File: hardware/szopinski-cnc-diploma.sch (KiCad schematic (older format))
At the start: 26 parts, among them J1 Barrel_Jack, J2 Conn_02x08_Odd_Even, J3 AVR-ISP-10, J4 Conn_01x04, J5 Conn_01x04, J6 Conn_01x04, J7 Conn_01x04, U1 ATmega328P-PU, U2 L7805, U3 DRV8825, U4 DRV8825, U5 DRV8825, U6 DRV8825, Y1 20 MHz

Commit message: Add custom symbol and footprint to project
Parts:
- removed U3, U4, U5, U6: DRV8825, Package_DIP:DIP-16_W15.24mm, symbol Driver_Motor:DRV8825
- added U3, U4, U5, U6: DRV8825, szopinski-cnc-diploma:DIP-16_W15.24mm, symbol drv8825:DRV8825
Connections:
- net +18V: now also U3.16 (VCC), U4.16 (VCC), U5.16 (VCC), U6.16 (VCC)
- net +5V: now also U3.2 (M0), U3.3 (M1), U3.4 (M2), U3.5 (~RST), U3.6 (~SLP), U4.2 (M0), U4.3 (M1), U4.4 (M2), U4.5 (~RST), U4.6 (~SLP), U5.2 (M0), U5.3 (M1), U5.4 (M2), U5.5 (~RST), U5.6 (~SLP), U6.2 (M0), U6.3 (M1), U6.4 (M2), U6.5 (~RST), U6.6 (~SLP)
- net DIR_X: now also U3.8 (DIR)
- net DIR_Y: now also U5.8 (DIR), U6.8 (DIR)
- net DIR_Z: now also U4.8 (DIR)
- net ENABLE_XY: now also U3.1 (~EN), U5.1 (~EN), U6.1 (~EN)
- net ENABLE_Z: now also U4.1 (~EN)
- net GND: now also U3.15 (GNDmot), U3.9 (GND), U4.15 (GNDmot), U4.9 (GND), U5.15 (GNDmot), U5.9 (GND), U6.15 (GNDmot), U6.9 (GND)
- net STEP_X: now also U3.7 (STEP)
- net STEP_Y: now also U5.7 (STEP), U6.7 (STEP)
- net STEP_Z: now also U4.7 (STEP)
- net at J4.1 (Pin_1): now also U3.14 (B2)
- net at J4.2 (Pin_2): now also U3.13 (B1)
- net at J4.3 (Pin_3): now also U3.12 (A1)
- net at J4.4 (Pin_4): now also U3.11 (A2)
- net at J6.1 (Pin_1): now also U5.14 (B2)
- net at J6.2 (Pin_2): now also U5.13 (B1)
- net at J6.3 (Pin_3): now also U5.12 (A1)
- net at J6.4 (Pin_4): now also U5.11 (A2)
- net at J5.1 (Pin_1): now also U4.14 (B2)
- net at J5.2 (Pin_2): now also U4.13 (B1)
- net at J5.3 (Pin_3): now also U4.12 (A1)
- net at J5.4 (Pin_4): now also U4.11 (A2)
- net at J7.1 (Pin_1): now also U6.14 (B2)
- net at J7.2 (Pin_2): now also U6.13 (B1)
- net at J7.3 (Pin_3): now also U6.12 (A1)
- net at J7.4 (Pin_4): now also U6.11 (A2)
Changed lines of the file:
@@
 NoConn ~ 9000 5050
 NoConn ~ 9000 2450
-$Comp
-L Driver_Motor:DRV8825 U3
-U 1 1 63106504
-P 6850 1700
-F 0 "U3" H 7528 1096 50  0000 L CNN
-F 1 "DRV8825" H 7528 1005 50  0000 L CNN
-F 2 "Package_DIP:DIP-16_W15.24mm" H 7550 1100 50  0001 C CNN
-F 3 "" H 7550 1100 50  0001 C CNN
-	1    6850 1700
-	1    0    0    -1
-$EndComp
-$Comp
-L Driver_Motor:DRV8825 U5
-U 1 1 6310708B
-P 9750 1700
-F 0 "U5" H 10428 1096 50  0000 L CNN
-F 1 "DRV8825" H 10428 1005 50  0000 L CNN
-F 2 "Package_DIP:DIP-16_W15.24mm" H 10450 1100 50  0001 C CNN
-F 3 "" H 10450 1100 50  0001 C CNN
-	1    9750 1700
-	1    0    0    -1
-$EndComp
-$Comp
-L Driver_Motor:DRV8825 U6
-U 1 1 63107951
-P 9750 4300
-F 0 "U6" H 10428 3696 50  0000 L CNN
-F 1 "DRV8825" H 10428 3605 50  0000 L CNN
-F 2 "Package_DIP:DIP-16_W15.24mm" H 10450 3700 50  0001 C CNN
-F 3 "" H 10450 3700 50  0001 C CNN
-	1    9750 4300
-	1    0    0    -1
-$EndComp
-$Comp
-L Driver_Motor:DRV8825 U4
-U 1 1 63108532
-P 6850 4300
-F 0 "U4" H 7528 3696 50  0000 L CNN
-F 1 "DRV8825" H 7528 3605 50  0000 L CNN
-F 2 "Package_DIP:DIP-16_W15.24mm" H 7550 3700 50  0001 C CNN
-F 3 "" H 7550 3700 50  0001 C CNN
-	1    6850 4300
-	1    0    0    -1
-$EndComp
 Text Label 5250 5400 2    50   Italic 0
 ENABLE_Z
@@
 NoConn ~ 2900 3300
 NoConn ~ 4900 4000
+$Comp
+L drv8825:DRV8825 U3
+U 1 1 631C04A9
+P 6850 1700
+F 0 "U3" H 7528 1096 50  0000 L CNN
+F 1 "DRV8825" H 7528 1005 50  0000 L CNN
+F 2 "szopinski-cnc-diploma:DIP-16_W15.24mm" H 7550 1100 50  0001 C CNN
+F 3 "" H 7550 1100 50  0001 C CNN
+	1    6850 1700
+	1    0    0    -1
+$EndComp
+$Comp
+L drv8825:DRV8825 U5
+U 1 1 631C0D6D
+P 9750 1700
+F 0 "U5" H 10428 1096 50  0000 L CNN
+F 1 "DRV8825" H 10428 1005 50  0000 L CNN
+F 2 "szopinski-cnc-diploma:DIP-16_W15.24mm" H 10450 1100 50  0001 C CNN
+F 3 "" H 10450 1100 50  0001 C CNN
+	1    9750 1700
+	1    0    0    -1
+$EndComp
+$Comp
+L drv8825:DRV8825 U4
+U 1 1 631C1F07
+P 6850 4300
+F 0 "U4" H 7528 3696 50  0000 L CNN
+F 1 "DRV8825" H 7528 3605 50  0000 L CNN
+F 2 "szopinski-cnc-diploma:DIP-16_W15.24mm" H 7550 3700 50  0001 C CNN
+F 3 "" H 7550 3700 50  0001 C CNN
+	1    6850 4300
+	1    0    0    -1
+$EndComp
+$Comp
+L drv8825:DRV8825 U6
+U 1 1 631C2F6C
+P 9750 4300
+F 0 "U6" H 10428 3696 50  0000 L CNN
+F 1 "DRV8825" H 10428 3605 50  0000 L CNN
+F 2 "szopinski-cnc-diploma:DIP-16_W15.24mm" H 10450 3700 50  0001 C CNN
+F 3 "" H 10450 3700 50  0001 C CNN
+	1    9750 4300
+	1    0    0    -1
+$EndComp
 $EndSCHEMATC

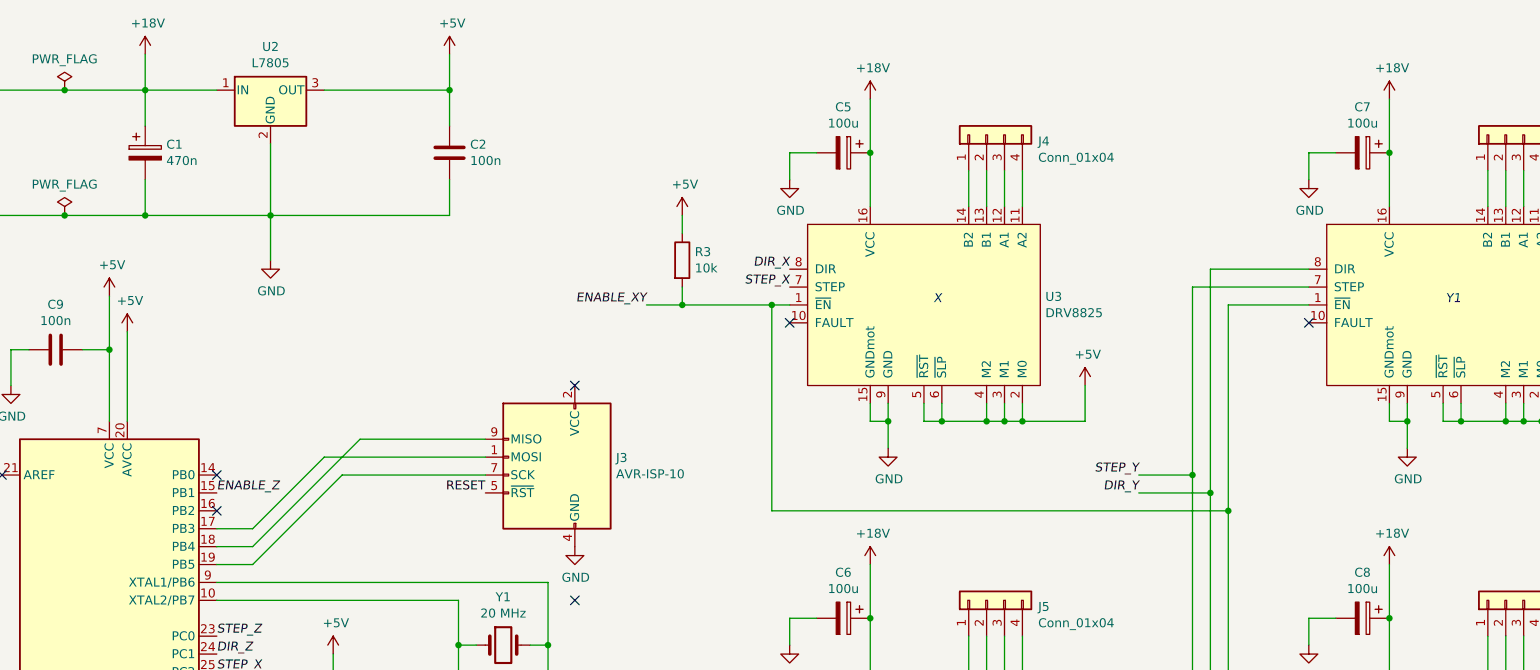
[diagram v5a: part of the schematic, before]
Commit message: Change 18V to 12V
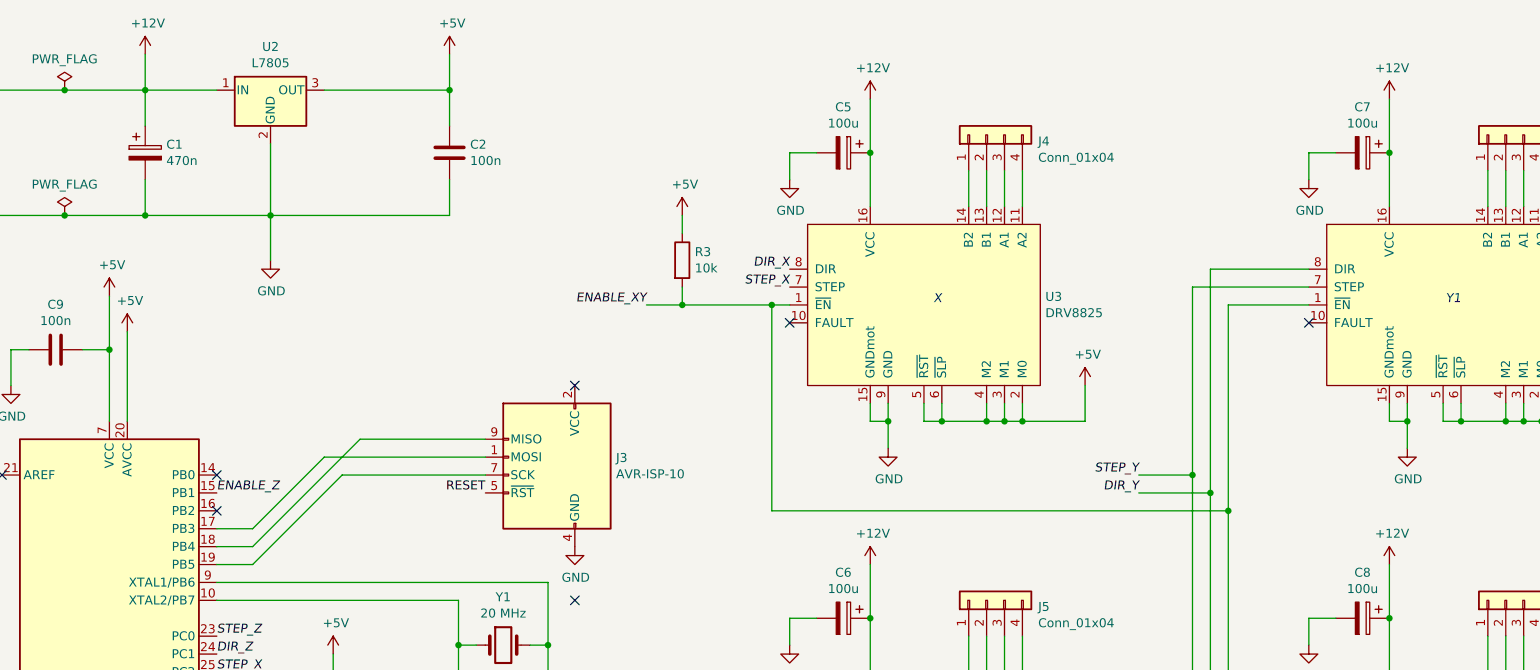
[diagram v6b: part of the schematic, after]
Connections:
- net +18V renamed +12V
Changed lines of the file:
@@
 	2500 1650 2500 1850
 Connection ~ 2500 1850
-$Comp
-L power:+18V #PWR0101
-U 1 1 62FB46FE
-P 2500 950
-F 0 "#PWR0101" H 2500 800 50  0001 C CNN
-F 1 "+18V" H 2515 1123 50  0000 C CNN
-F 2 "" H 2500 950 50  0001 C CNN
-F 3 "" H 2500 950 50  0001 C CNN
-	1    2500 950
-	1    0    0    -1
-$EndComp
 Wire Wire Line
 	1650 1850 2050 1850
@@
 Wire Wire Line
 	3550 4400 3550 4300
-$Comp
-L power:+18V #PWR0108
-U 1 1 6300C248
-P 6550 1200
-F 0 "#PWR0108" H 6550 1050 50  0001 C CNN
-F 1 "+18V" H 6565 1373 50  0000 C CNN
-F 2 "" H 6550 1200 50  0001 C CNN
-F 3 "" H 6550 1200 50  0001 C CNN
-	1    6550 1200
-	1    0    0    -1
-$EndComp
 Wire Wire Line
 	2900 3900 4750 3900
@@
 $EndComp
 $Comp
-L power:+18V #PWR0114
-U 1 1 6303BF41
-P 9450 1200
-F 0 "#PWR0114" H 9450 1050 50  0001 C CNN
-F 1 "+18V" H 9465 1373 50  0000 C CNN
-F 2 "" H 9450 1200 50  0001 C CNN
-F 3 "" H 9450 1200 50  0001 C CNN
-	1    9450 1200
-	1    0    0    -1
-$EndComp
-$Comp
 L Device:CP C7
 U 1 1 6303BF4D
@@
 $EndComp
 $Comp
-L power:+18V #PWR0118
-U 1 1 63053EDC
-P 6550 3800
-F 0 "#PWR0118" H 6550 3650 50  0001 C CNN
-F 1 "+18V" H 6565 3973 50  0000 C CNN
-F 2 "" H 6550 3800 50  0001 C CNN
-F 3 "" H 6550 3800 50  0001 C CNN
-	1    6550 3800
-	1    0    0    -1
-$EndComp
-$Comp
 L Device:CP C6
 U 1 1 63053EE8
@@
 F 3 "" H 7750 5400 50  0001 C CNN
 	1    7750 5400
-	1    0    0    -1
-$EndComp
-$Comp
-L power:+18V #PWR0122
-U 1 1 63053F31
-P 9450 3800
-F 0 "#PWR0122" H 9450 3650 50  0001 C CNN
-F 1 "+18V" H 9465 3973 50  0000 C CNN
-F 2 "" H 9450 3800 50  0001 C CNN
-F 3 "" H 9450 3800 50  0001 C CNN
-	1    9450 3800
 	1    0    0    -1
 $EndComp
@@
 	1    0    0    -1
 $EndComp
+$Comp
+L power:+12V #PWR?
+U 1 1 62FEF948
+P 2500 950
+F 0 "#PWR?" H 2500 800 50  0001 C CNN
+F 1 "+12V" H 2515 1123 50  0000 C CNN
+F 2 "" H 2500 950 50  0001 C CNN
+F 3 "" H 2500 950 50  0001 C CNN
+	1    2500 950
+	1    0    0    -1
+$EndComp
+$Comp
+L power:+12V #PWR?
+U 1 1 62FF0287
+P 6550 1200
+F 0 "#PWR?" H 6550 1050 50  0001 C CNN
+F 1 "+12V" H 6565 1373 50  0000 C CNN
+F 2 "" H 6550 1200 50  0001 C CNN
+F 3 "" H 6550 1200 50  0001 C CNN
+	1    6550 1200
+	1    0    0    -1
+$EndComp
+$Comp
+L power:+12V #PWR?
+U 1 1 62FF0BDD
+P 9450 1200
+F 0 "#PWR?" H 9450 1050 50  0001 C CNN
+F 1 "+12V" H 9465 1373 50  0000 C CNN
+F 2 "" H 9450 1200 50  0001 C CNN
+F 3 "" H 9450 1200 50  0001 C CNN
+	1    9450 1200
+	1    0    0    -1
+$EndComp
+$Comp
+L power:+12V #PWR?
+U 1 1 62FF0F2C
+P 9450 3800
+F 0 "#PWR?" H 9450 3650 50  0001 C CNN
+F 1 "+12V" H 9465 3973 50  0000 C CNN
+F 2 "" H 9450 3800 50  0001 C CNN
+F 3 "" H 9450 3800 50  0001 C CNN
+	1    9450 3800
+	1    0    0    -1
+$EndComp
+$Comp
+L power:+12V #PWR?
+U 1 1 62FF1485
+P 6550 3800
+F 0 "#PWR?" H 6550 3650 50  0001 C CNN
+F 1 "+12V" H 6565 3973 50  0000 C CNN
+F 2 "" H 6550 3800 50  0001 C CNN
+F 3 "" H 6550 3800 50  0001 C CNN
+	1    6550 3800
+	1    0    0    -1
+$EndComp

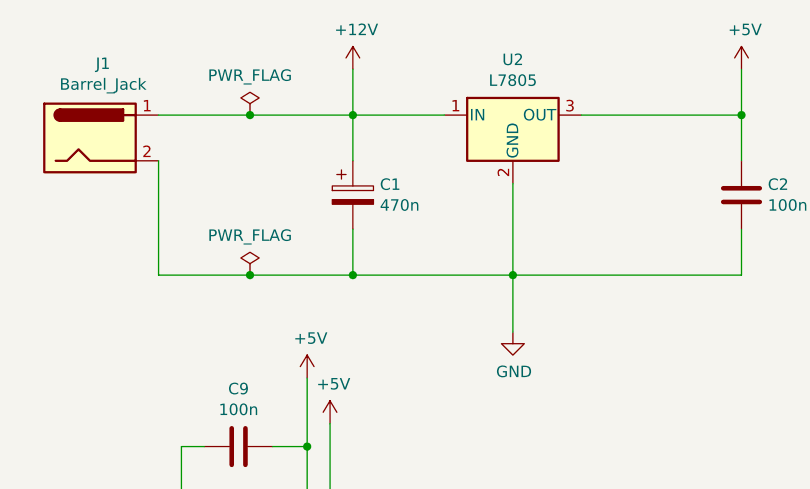
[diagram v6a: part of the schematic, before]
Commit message: Increase input capacitor value
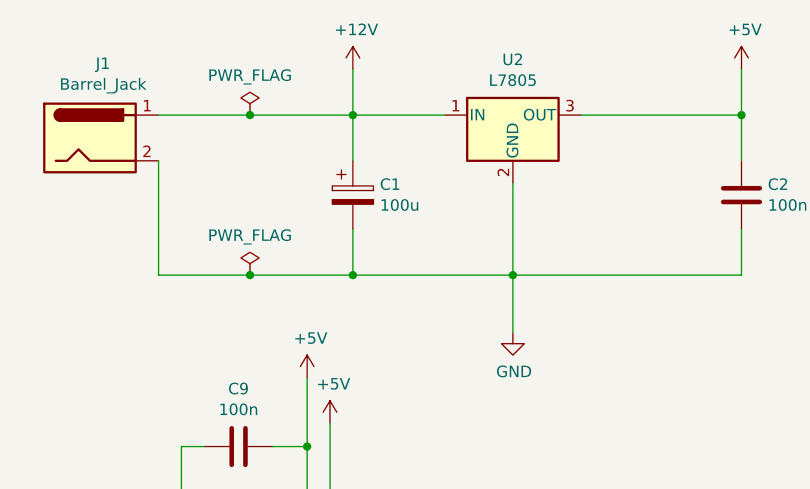
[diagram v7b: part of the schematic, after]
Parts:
- C1: value 470n -> 100u; footprint Capacitor_THT:CP_Radial_D4.0mm_P1.50mm -> Capacitor_THT:CP_Radial_D6.3mm_P2.50mm
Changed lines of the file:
@@
 P 2500 1500
 F 0 "C1" H 2618 1546 50  0000 L CNN
-F 1 "470n" H 2618 1455 50  0000 L CNN
-F 2 "Capacitor_THT:CP_Radial_D4.0mm_P1.50mm" H 2538 1350 50  0001 C CNN
+F 1 "100u" H 2618 1455 50  0000 L CNN
+F 2 "Capacitor_THT:CP_Radial_D6.3mm_P2.50mm" H 2538 1350 50  0001 C CNN
 F 3 "~" H 2500 1500 50  0001 C CNN
 	1    2500 1500

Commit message: Advisor review
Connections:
- no-connect marks 26 -> 25
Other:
- note added: "In-system programming"
- note added: "Microcontroller"
- note added: "Power supply"
- note added: "Serial interface\n(FT232R breakout board)"
- note added: "Stepper motor drivers"
- moved on the sheet: C3, C4, C9, J2, J3, R1, U1, Y1
